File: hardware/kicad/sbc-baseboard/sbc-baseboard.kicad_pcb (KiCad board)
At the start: 4 copper layers, 140 x 80 mm, 339 parts, among them J1 USB-C upstream, J10 RJ45 magjack 10/100, J11 COM/NO/NC, J12 COM/NO/NC, J13 Console, J14 +5V_TGT out, J15 GPIO + I2C, J16 SWD, J17 Qwiic PD, J18 PSU in (isolated), J19 PSU out (isolated), J2 USB-C PD in, J3 USB-C HID to target, J4 USB-A x2, J5 USB-A x2, J601 SWD (K20), J9 FTDI header, K801 G6K-2F-Y DC5, K802 G6K-2F-Y DC5, K803 JW1FSN-DC5V, Q101 2N7002, Q102 2N7002, Q801 2N7002, Q802 2N7002, Q803 AO3400A, SW201 RESET, SW601 DAP RESET, U101 STUSB4500QTR, U102 PCA9517A, U103 TPS54560BDDA, U104 TPS54560BDDA, U105 TPS62823DLC, U201 MK64FN1M0VLL12, U202 USBLC6-2SC6, U301 KSZ8081RNA, U401 USBLC6-2SC6, U402 USB2517, U403 TPS2553DBV, U404 TPS2553DBV, U405 TPS2553DBV, U406 TPS2553DBV, U407 TPS2553DBV, U408 USBLC6-2SC6, U409 USBLC6-2SC6, U410 USBLC6-2SC6, U411 USBLC6-2SC6, U501 FT231XS, U601 MK20DX128VFM5, U701 TXB0104PW, U702 TXB0108PW, U703 TXS0102DCU, U704 TPS26630RGE, U801 LTV-817, Y201 32.768kHz, Y301 25MHz, Y401 24MHz, Y601 8MHz

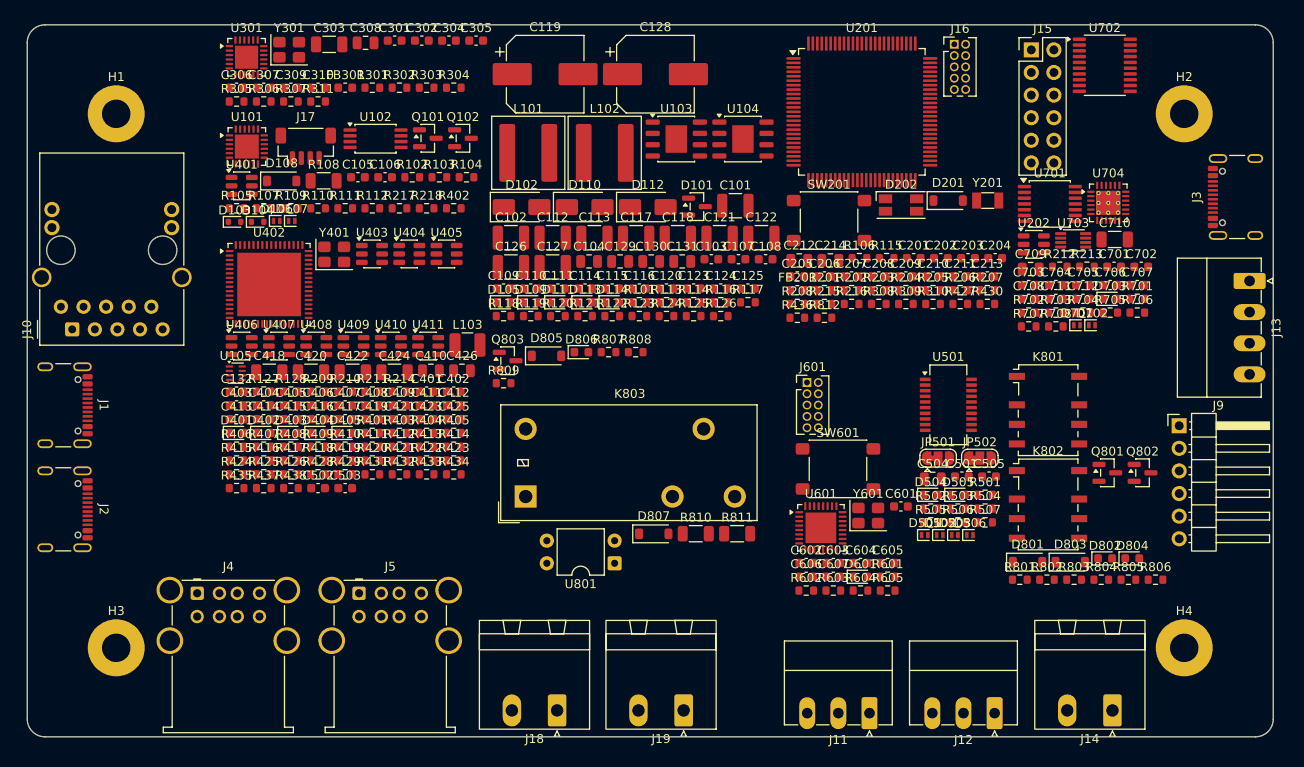
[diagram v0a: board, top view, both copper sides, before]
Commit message: Layout guidelines per IC; connectors mate from the pins-at-the-rear rule; edge zone and body spacing per the layout standard
docs/layout-guidelines.md: each IC's datasheet layout rules with their source
(TPS54560B, TPS62823, TPS2553, TPS2663 layout sections; USB2517 hardware
design checklist; KSZ8081 magnetics and decoupling; FT231X and STUSB4500 to
confirm) and how the board meets them. The generator derives every edge
connector's mating direction from the rule that the solder pins sit at the
rear of a horizontal connector: the RJ45 now faces outward instead of the
mounting hole. Interior parts keep 3 mm from the edges and 0.6 mm between
bodies (ECSS-Q-ST-70-12C 14.3, tailored as the directives record). DRC
unchanged: twelve errors inside the USB-C footprints, 499 unrouted.

Co-Authored-By: Claude Fable 5.1 <noreply@anthropic.com>
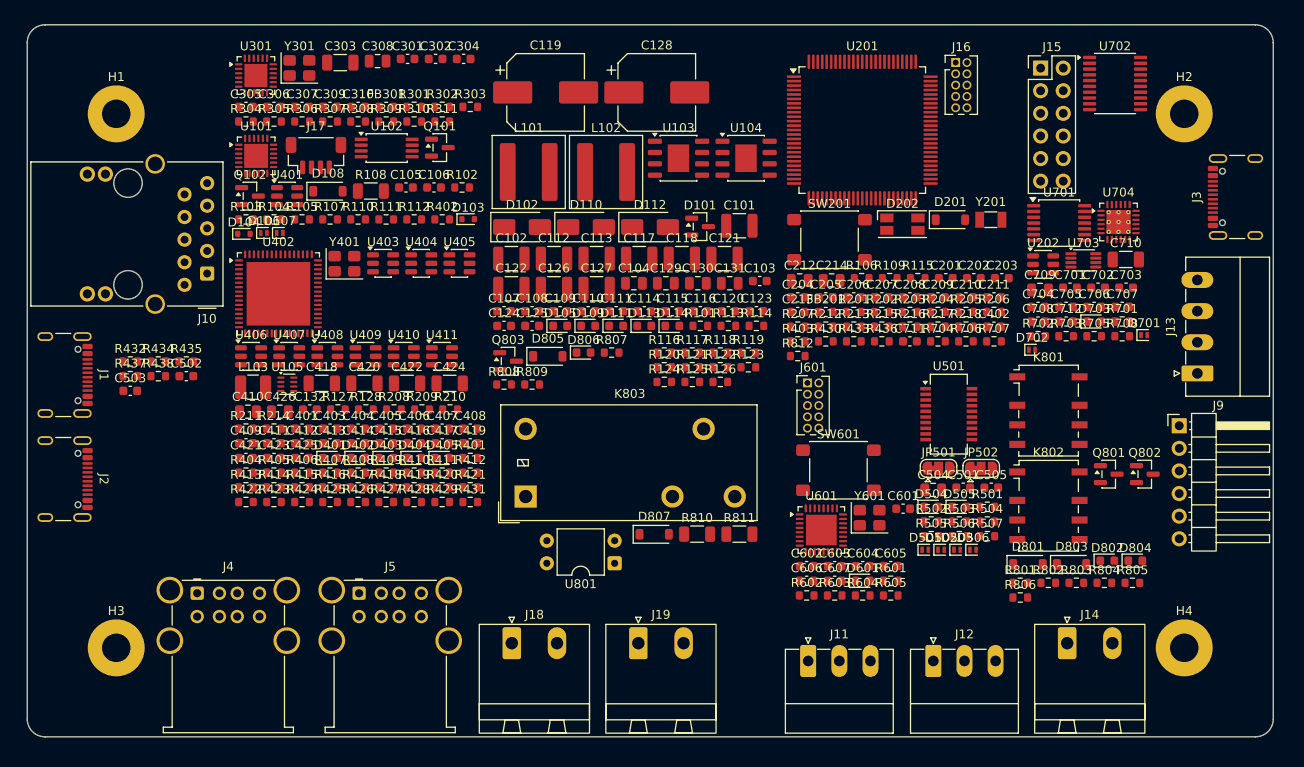
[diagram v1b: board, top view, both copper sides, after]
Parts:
- moved R427 68.2 mm to (40.3, 53.6)
- moved R109 67.7 mm to (96.9, 28.5)
- moved R218 62.0 mm to (105.5, 33.9)
- moved R308 62.0 mm to (37.2, 10.9)
- moved R217 61.9 mm to (102.3, 33.9)
- moved R309 61.9 mm to (40.3, 10.9)
- moved R310 61.8 mm to (43.5, 10.9)
- moved C402 61.1 mm to (108.6, 33.9)
- moved R433 50.3 mm to (92.9, 35.6)
- moved R208 46.8 mm to (41.2, 43.2)
- moved R403 45.9 mm to (86.6, 35.6)
- moved R434 35.5 mm to (14.7, 37.8)
- moved R432 32.8 mm to (11.6, 37.8)
- moved C122 28.7 mm to (54.4, 29.7)
- moved R212 27.1 mm to (89.7, 33.9)
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
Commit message: Placement pass per the layout standard: connectors locked, holes at 7 mm, ICs anchored, every other part at the pin it serves
gen/pcb.py places by ecad-standards/layout.md section 3: the edge connectors
stay where the directives put them; the mounting holes move out to 7 mm from
each corner (10.5 mm corner keep-outs); the ICs are anchored by flow in
gen/layout.py and the generator refuses an anchor table that overlaps or
stands in a keep-out; every other part is placed at the pin it serves, its
host the placed part it shares the most specific nets with (a decoupling
capacitor's host is the IC the schematic draws it beside), on the host's
nearest side, two-pin parts turned to face it, packed outward in rings, in
five passes (small decoupling, the large parts on the pins, bulk, the small
parts on the pins, passive-hosted), with the nearest free spot as the
fallback. The silkscreen pass places every designator where it overlaps
nothing and omits it otherwise; ICs and connectors are never omitted.
placement.txt records every part's host and ring.

The board file, the DRC report and the placement report are byte-identical
between generations: footprints, graphics and zones are written in a sorted
order with UUIDs derived in document order, the DRC report's entries are
sorted and the USB-C's coincident pads named one way.

DRC: 12 errors, all the documented GCT USB-C hole clearances; 499 unrouted;
zero warnings. Directives, spec, README and the root-sheet note updated for
the 7 mm holes and the placement method.

Co-Authored-By: Claude Fable 5.1 <noreply@anthropic.com>
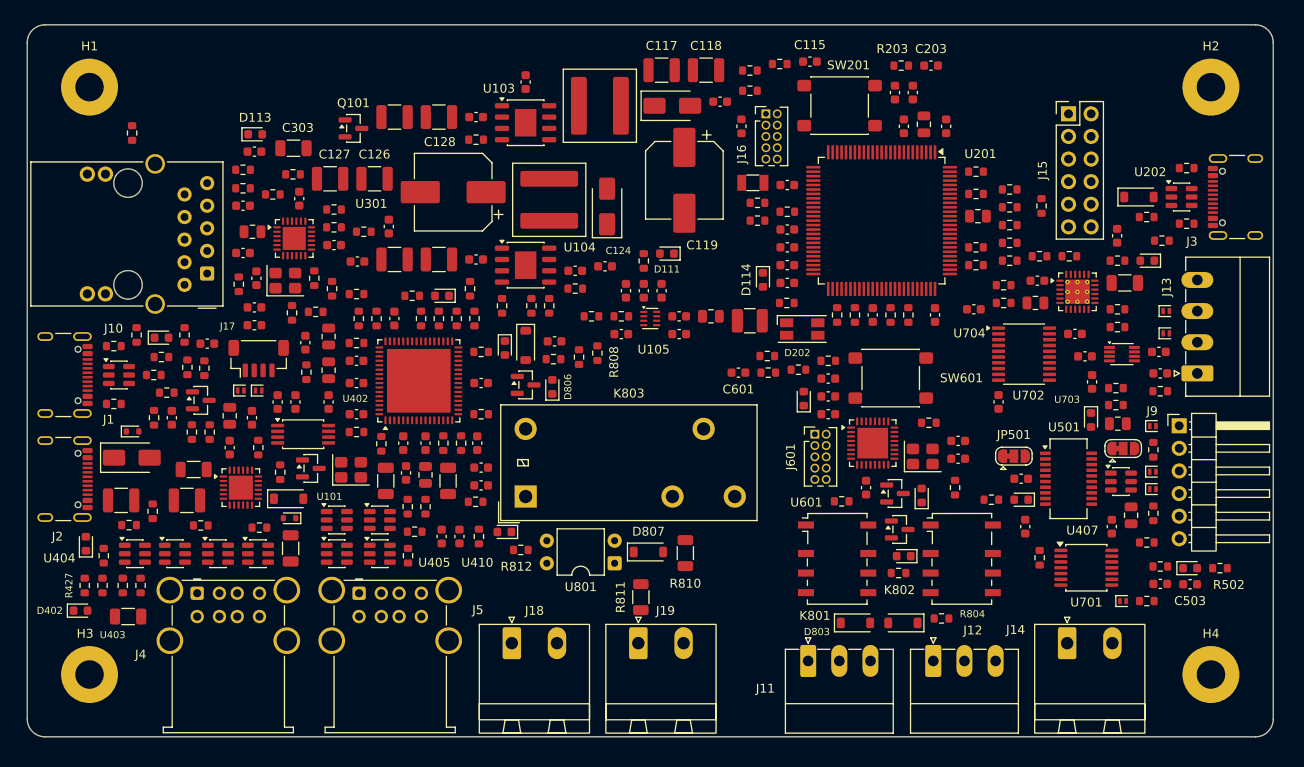
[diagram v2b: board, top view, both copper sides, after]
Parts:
- moved C503 121.1 mm to (130.7, 62.9)
- moved R437 116.0 mm to (126.5, 54.9), turned to -90 degrees
- moved R438 112.1 mm to (126.5, 47.7), turned to 90 degrees
- moved C502 101.8 mm to (119.6, 40.1), turned to 90 degrees
- moved C426 96.3 mm to (124.0, 55.1), turned to -90 degrees
- moved R211 94.5 mm to (117.1, 26.0)
- moved U407 94.5 mm to (122.9, 51.3)
- moved R109 89.9 mm to (11.4, 56.2)
- moved R214 85.8 mm to (110.4, 22.5)
- moved R106 81.0 mm to (14.2, 44.1), turned to -90 degrees
- moved C101 76.0 mm to (10.6, 53.4)
- moved D405 73.0 mm to (119.5, 44.4), turned to -90 degrees
- moved R210 68.4 mm to (113.7, 26.0)
- moved R209 68.1 mm to (110.4, 26.5)
- moved R208 67.4 mm to (106.6, 27.0)
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
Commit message: Lanes and two-sided placement: the PSU passthrough lanes laid and kept clear, small passives under the pins they serve
Lanes (gen/layout.py LANES): a corridor reserved for one routed path, from
pad to pad through axis-aligned legs, as wide as the class track plus
clearance plus 0.25 mm, kept free of parts on both sides (footprint keep-out
rule areas stopping at the parts the lane joins) and laid as copper at the
class width. Two lanes carry the passthrough: J18 pin 1 to K803 COM and
K803 NO to J19 pin 1, 2 mm PSU_3A tracks; PSU_GND goes through the L2
island. The generator refuses a lane with a diagonal leg, a pad off its net
or a fixed part in its way.

Sides: connectors, ICs, relays, inductors, crystals, switches, jumpers,
LEDs, large parts and everything on a current-carrying, pair or
switching-loop net stay on top; resistors and capacitors up to 1206, small
diodes and SOT-23 transistors go to the bottom, tucked 1 mm under their
host's pin row, clear of through-hole pads (1 mm) and exposed-pad via
fields (0.6 mm), the top as their fallback. 126 of 339 parts are on the
bottom; the silkscreen pass runs on both sides.

The L2 ground plane is now one outline notched around the isolation
region: a zone outline with a hole does not fill in KiCad, which the DRC
gate's new zone refill exposed (the plane was 30 mm2). The isolation rules
keep board-net tracks and vias out of the region, forbid a board-net zone
inside it, and exempt no-net pads (the relay's NC contact) from the creepage
clearance. DRC: 12 documented errors, zero warnings; board, DRC report and
placement report reproducible.

Co-Authored-By: Claude Fable 5.1 <noreply@anthropic.com>
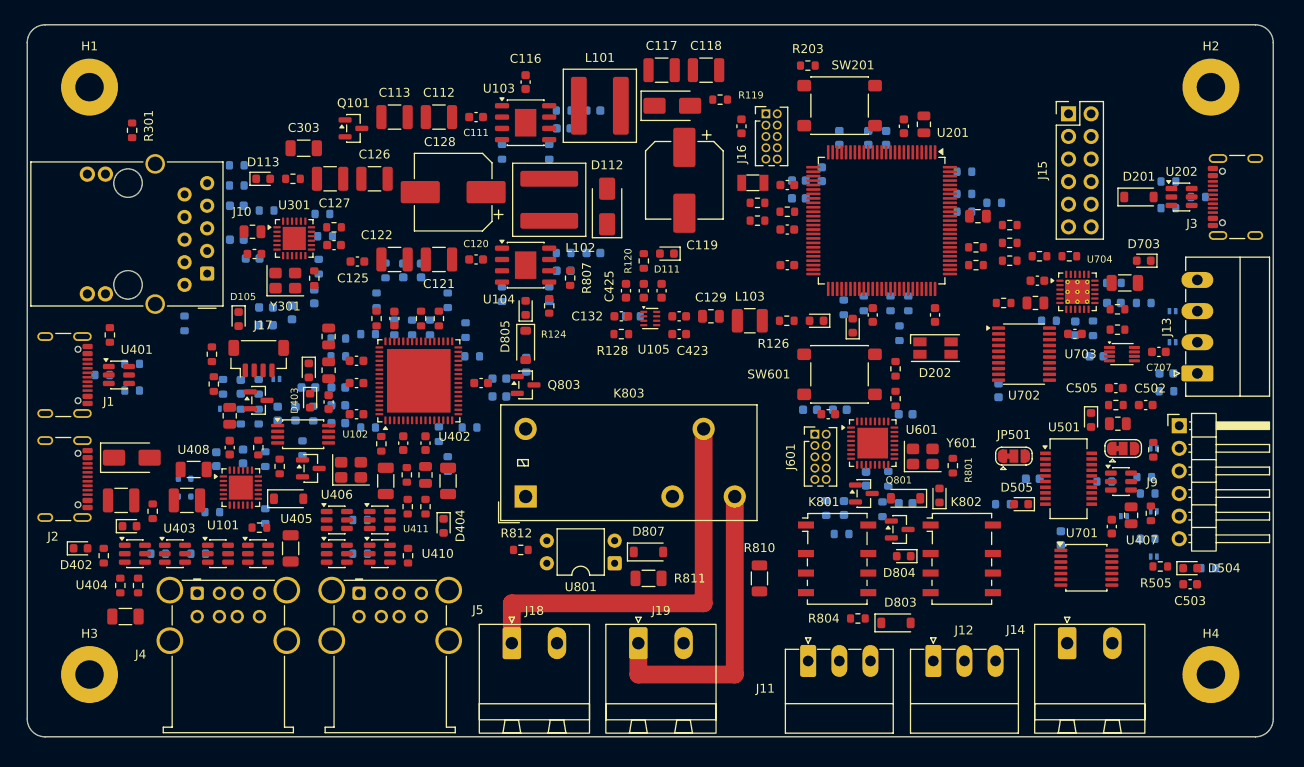
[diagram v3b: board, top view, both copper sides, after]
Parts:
- C105, C106, C107, C108, C109, C114, C115, C123, C124, C201, C202, C203, C204, C205, C213, C301, C302, C304, C305, C306, C307, C309, C401, C402, C411, C412, C413, C414, C415, C416, C501, C601, C602, C603, C604, C606, C607, C701, C702, C704, C706, C711, C712, D103, D104, D106, D107, D501, D502, D503, D506, D701, D702, R102, R104, R105, R106, R109, R111, R112, R113, R114, R115, R116, R117, R118, R121, R122, R123, R127, R201, R202, R205, R206, R207, R215, R216, R303, R304, R305, R306, R307, R308, R311, R401, R402, R404, R405, R406, R407, R412, R413, R414, R415, R416, R417, R418, R419, R420, R421, R422, R423, R425, R428, R431, R434, R437, R501, R502, R503, R506, R507, R601, R604, R605, R701, R702, R705, R707, R708, R802, R803, R805, R806, R808, R809: moved to B.Cu
- moved D403 26.3 mm to (31.8, 42.2), turned to -90 degrees
- moved C115 24.9 mm to (63.6, 9.63)
- moved R403 24.9 mm to (46.2, 33.0), turned to -90 degrees
- moved C416 23.8 mm to (31.6, 40.8), turned to 180 degrees
- moved R118 23.6 mm to (58.6, 14.3), turned to -90 degrees
- moved C505 22.6 mm to (122.3, 40.8)
- moved R117 21.4 mm to (60.3, 9.63)
- moved R401 21.3 mm to (40.2, 27.6), turned to 90 degrees
- moved D404 21.1 mm to (46.8, 56.3)
- moved C415 20.4 mm to (35.0, 40.8), turned to 180 degrees
- moved R111 19.8 mm to (30.9, 47.6)
- moved C601 19.3 mm to (91.8, 54.3), turned to -90 degrees
- moved C114 17.8 mm to (60.3, 11.6)
- moved C203 17.3 mm to (89.3, 16.8), turned to -90 degrees
- moved R114 17.3 mm to (32.1, 43.7), turned to 90 degrees
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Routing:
- net /Relays/PSU_VP: track 0.00 -> 45.6 mm
- net /Relays/PSU_VOUT: track 0.00 -> 34.4 mm

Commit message: ESD in line at the connectors, every USB 2.0 pair net in the 90 ohm class
The hub-side halves of the pairs through the USBLC6-2 arrays (HUB_UP,
HUB_DN4-7) were sheet-local nets that the USB class patterns did not
match, so they sat in the Default class; the patterns now start with *,
and build.py refuses a build in which a _P/_N pair is outside a pair class.
gen/pcb.py recognises ESD parts by value, keeps them on top, places them
first of all at their connector's signal pins, and turns a flow-through
array so its connector-side pins face the connector; it reports each ESD
part's place and facing. Directives, guideline table and README updated
for ecad-standards/layout.md 3.8.

Co-Authored-By: Claude Fable 5.1 <noreply@anthropic.com>
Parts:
- D103, D104, D106, D107, D501, D502, D503, D506, D701, D702: moved to F.Cu
- moved D403 19.4 mm to (49.8, 49.3)
- moved R430 17.2 mm to (43.3, 57.0), turned to 180 degrees
- moved D402 16.6 mm to (17.1, 46.5), turned to -90 degrees
- moved R108 15.0 mm to (31.8, 57.3), turned to 90 degrees
- moved R429 14.4 mm to (19.1, 49.8)
- moved C426 11.7 mm to (118.8, 44.7), turned to 180 degrees
- moved R438 11.6 mm to (115.2, 45.2), turned to 180 degrees
- moved D105 11.5 mm to (15.2, 40.8)
- moved D806 9.37 mm to (59.0, 40.7)
- moved R427 9.11 mm to (16.8, 56.5), turned to 180 degrees
- moved R807 9.10 mm to (59.0, 37.3)
- moved R101 9.01 mm to (15.2, 44.1)
- moved D401 8.28 mm to (16.6, 49.8), turned to -90 degrees
- moved D104 8.26 mm to (19.7, 45.0)
- moved D405 7.74 mm to (111.8, 45.2), turned to 0 degrees
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
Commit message: RJ45 to the back edge, the USB-C inlets spread around the middle of the left edge
J10 now sits on the back edge from x = 14, facing out; J2 (PD in) is
centred at y = 30 and J1 (upstream) at y = 54, split around the middle of
the left edge, so the lower-left corner carries only J1's protection and
the USB-A port band. The PHY turned to face the jack above it; the PD
controller, its bus buffer and the programming header moved up with J2.
The back edge no longer lies flat against a wall or rail, which the spec
and the directives record. DRC unchanged: 12 documented errors, zero
warnings; board reproducible.

Co-Authored-By: Claude Fable 5.1 <noreply@anthropic.com>
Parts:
- moved R108 28.4 mm to (8.25, 41.3)
- moved C102 26.0 mm to (17.9, 27.4)
- moved R301 23.4 mm to (34.9, 8.30), turned to 0 degrees
- moved C101 23.2 mm to (17.9, 31.4)
- moved R302 23.2 mm to (11.9, 11.8), turned to 180 degrees
- moved D102 21.0 mm to (11.8, 27.6)
- moved J2 21.0 mm to (3.10, 30.0)
- moved C420 20.0 mm to (22.1, 49.8), turned to 90 degrees
- moved C307 19.4 mm to (13.3, 26.2), turned to 180 degrees
- moved C303 19.3 mm to (14.7, 24.1), turned to 180 degrees
- moved D105 19.1 mm to (7.15, 23.5), turned to 0 degrees
- moved R102 18.4 mm to (11.8, 38.8)
- moved C103 18.4 mm to (13.8, 31.5)
- moved C105 18.4 mm to (15.2, 32.5)
- moved C106 18.4 mm to (12.2, 32.8)
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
